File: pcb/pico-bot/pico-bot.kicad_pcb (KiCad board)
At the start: 2 copper layers, 101.6 x 1.7 mm, 62 parts, among them J1 Conn_01x02_Male, J2 Conn_01x06_Male, J3 Conn_01x06_Male, J4 Conn_01x06_Male, J5 Conn_01x06_Male, Q1 DMG2305UX, Q2 AOD417, SW1 SW_SPDT, SW2 SW_Push, SW3 SW_Push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

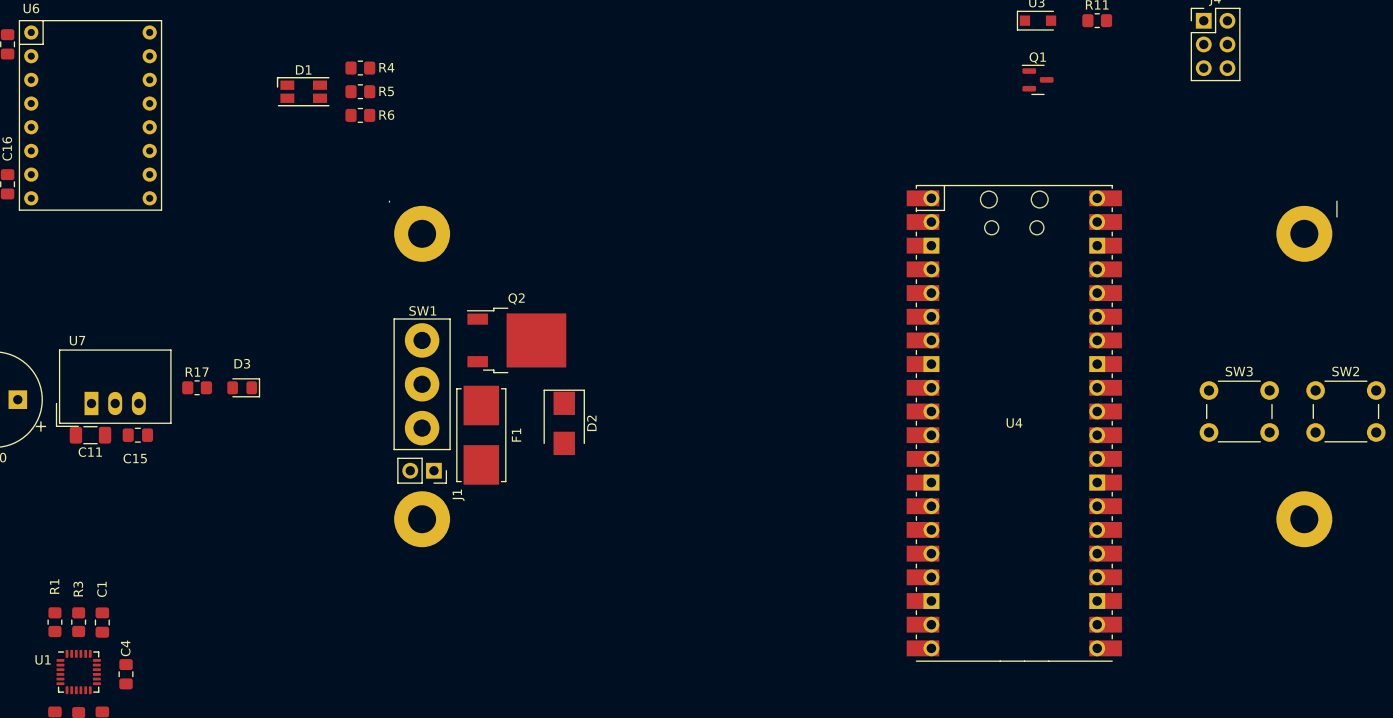
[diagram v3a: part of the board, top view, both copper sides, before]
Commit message: Add rough board outline
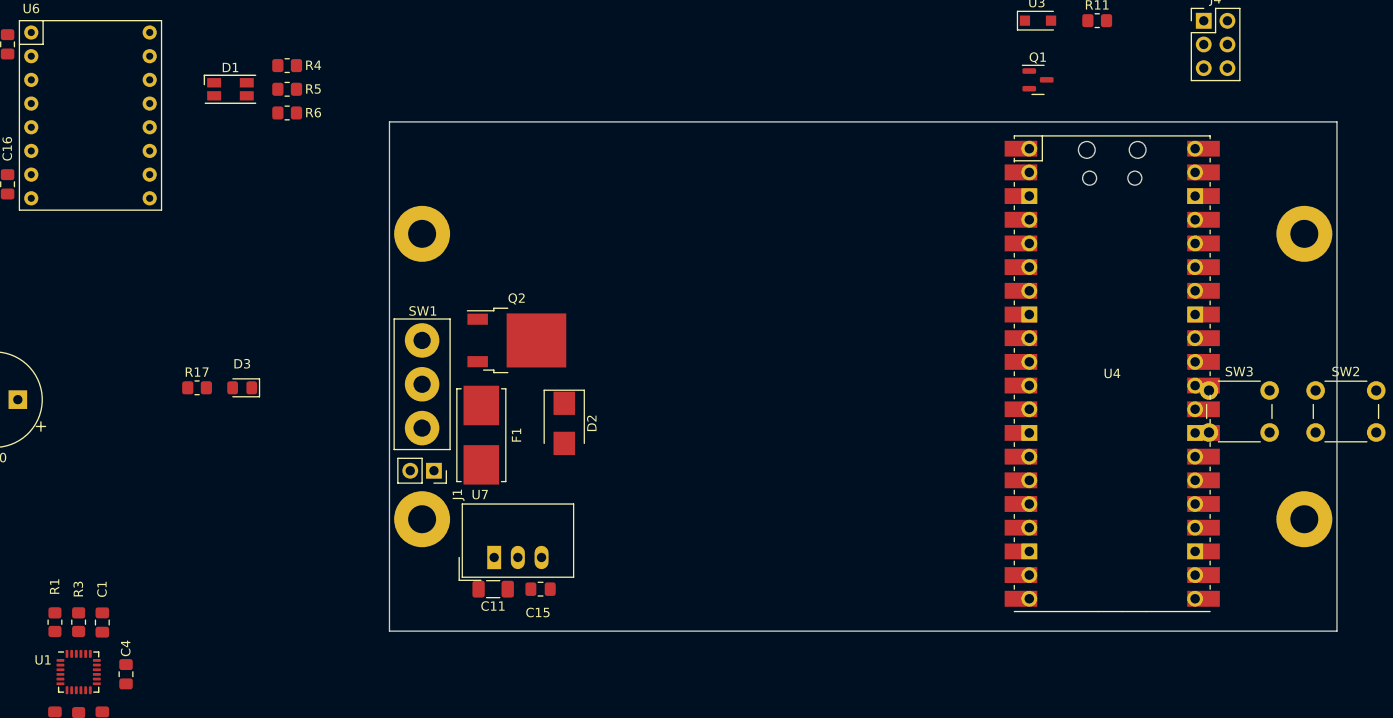
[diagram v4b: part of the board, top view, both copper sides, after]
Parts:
- moved C11 46.2 mm to (108.5, 116.6)
- moved C15 46.2 mm to (113.6, 116.6)
- moved U7 46.2 mm to (108.6, 113.2)
- moved U4 11.8 mm to (174.9, 93.5)
- moved D1 7.85 mm to (80.3, 63.0)
- moved R4 7.85 mm to (86.4, 60.5)
- moved R5 7.85 mm to (86.4, 63.0)
- moved R6 7.85 mm to (86.4, 65.5)
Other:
- board size 101.6 x 1.7 mm -> 101.6 x 54.6 mm
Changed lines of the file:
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@@
   )
   (footprint "pico-bot:RPi_Pico_SMD_TH" (layer "F.Cu")
-    (at 164.4 98.82)
+    (at 174.9 93.5)
     (descr "Through hole straight pin header, 2x20, 2.54mm pitch, double rows")
     (tags "Through hole pin header THT 2x20 2.54mm double row")
@@
   )
   (footprint "LED_SMD:LED_RGB_1210" (layer "F.Cu")
-    (at 88.2 63.26)
+    (at 80.35 63)
     (descr "RGB LED 3.2x2.7mm http://www.avagotech.com/docs/AV02-0610EN")
     (tags "LED 3227")
@@
   )
   (footprint "Resistor_SMD:R_0805_2012Metric_Pad1.20x1.40mm_HandSolder" (layer "F.Cu")
-    (at 94.28 60.72)
+    (at 86.43 60.46)
     (descr "Resistor SMD 0805 (2012 Metric), square (rectangular) end terminal, IPC_7351 nominal with elongated pad for handsoldering. (Body size source: IPC-SM-782 page 72, https://www.pcb-3d.com/wordpress/wp-content/uploads/ipc-sm-782a_amendment_1_and_2.pdf), generated with kicad-footprint-generator")
     (tags "resistor handsolder")
@@
   )
   (footprint "Capacitor_SMD:C_1206_3216Metric_Pad1.33x1.80mm_HandSolder" (layer "F.Cu")
-    (at 65.34 100.09 180)
+    (at 108.52 116.6 180)
     (descr "Capacitor SMD 1206 (3216 Metric), square (rectangular) end terminal, IPC_7351 nominal with elongated pad for handsoldering. (Body size source: IPC-SM-782 page 76, https://www.pcb-3d.com/wordpress/wp-content/uploads/ipc-sm-782a_amendment_1_and_2.pdf), generated with kicad-footprint-generator")
     (tags "capacitor handsolder")
@@
   )
   (footprint "Converter_DCDC:Converter_DCDC_TRACO_TSR-1_THT" (layer "F.Cu")
-    (at 65.4475 96.6925)
+    (at 108.6275 113.2025)
     (descr "DCDC-Converter, TRACO, TSR 1-xxxx")
     (tags "DCDC-Converter TRACO TSR-1")
@@
   )
   (footprint "Capacitor_SMD:C_0805_2012Metric_Pad1.18x1.45mm_HandSolder" (layer "F.Cu")
-    (at 70.42 100.09)
+    (at 113.6 116.6)
     (descr "Capacitor SMD 0805 (2012 Metric), square (rectangular) end terminal, IPC_7351 nominal with elongated pad for handsoldering. (Body size source: IPC-SM-782 page 76, https://www.pcb-3d.com/wordpress/wp-content/uploads/ipc-sm-782a_amendment_1_and_2.pdf, https://docs.google.com/spreadsheets/d/1BsfQQcO9C6DZCsRaXUlFlo91Tg2WpOkGARC1WS5S8t0/edit?usp=sharing), generated with kicad-footprint-generator")
     (tags "capacitor handsolder")
@@
   )
   (footprint "Resistor_SMD:R_0805_2012Metric_Pad1.20x1.40mm_HandSolder" (layer "F.Cu")
-    (at 94.28 65.8)
+    (at 86.43 65.54)
     (descr "Resistor SMD 0805 (2012 Metric), square (rectangular) end terminal, IPC_7351 nominal with elongated pad for handsoldering. (Body size source: IPC-SM-782 page 72, https://www.pcb-3d.com/wordpress/wp-content/uploads/ipc-sm-782a_amendment_1_and_2.pdf), generated with kicad-footprint-generator")
     (tags "resistor handsolder")
@@
   )
   (footprint "Resistor_SMD:R_0805_2012Metric_Pad1.20x1.40mm_HandSolder" (layer "F.Cu")
-    (at 94.28 63.26)
+    (at 86.43 63)
     (descr "Resistor SMD 0805 (2012 Metric), square (rectangular) end terminal, IPC_7351 nominal with elongated pad for handsoldering. (Body size source: IPC-SM-782 page 72, https://www.pcb-3d.com/wordpress/wp-content/uploads/ipc-sm-782a_amendment_1_and_2.pdf), generated with kicad-footprint-generator")
     (tags "resistor handsolder")
@@
     )
   )
-  (gr_line (start 199 76.7) (end 199 75) (layer "Edge.Cuts") (width 0.1))
-  (gr_line (start 97.4 75.1) (end 97.4 75) (layer "Edge.Cuts") (width 0.1))
+  (gr_line (start 199 66.5) (end 97.4 66.5) (layer "Edge.Cuts") (width 0.1))
+  (gr_line (start 199 121.1) (end 199 66.5) (layer "Edge.Cuts") (width 0.1))
+  (gr_line (start 97.4 66.5) (end 97.4 121.1) (layer "Edge.Cuts") (width 0.1))
+  (gr_line (start 97.4 121.1) (end 199 121.1) (layer "Edge.Cuts") (width 0.1))
 )

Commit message: Finish init placement of components
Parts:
- moved J5 146.1 mm to (184.1, 117.2), turned to 90 degrees
- moved C19 123.3 mm to (144.1, 116.6), turned to 0 degrees
- moved J3 122.4 mm to (137.7, 113.4), turned to 90 degrees
- moved D1 121.6 mm to (195.5, 102.0), turned to -90 degrees
- moved R4 113.0 mm to (190.4, 104.5), turned to 180 degrees
- moved R5 111.1 mm to (190.4, 102.0), turned to 180 degrees
- moved R6 109.4 mm to (190.4, 99.5), turned to 180 degrees
- moved C18 101.1 mm to (143.4, 69.6), turned to 0 degrees
- moved J2 99.5 mm to (137.1, 72.8), turned to 90 degrees
- moved C14 93.2 mm to (142.2, 103.3)
- moved C12 93.2 mm to (137.1, 103.3)
- moved C13 93.2 mm to (139.6, 103.3)
- moved C2 90.8 mm to (146.6, 99.1)
- moved C3 90.8 mm to (151.7, 99.1)
- moved R1 90.8 mm to (146.6, 88.4)
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
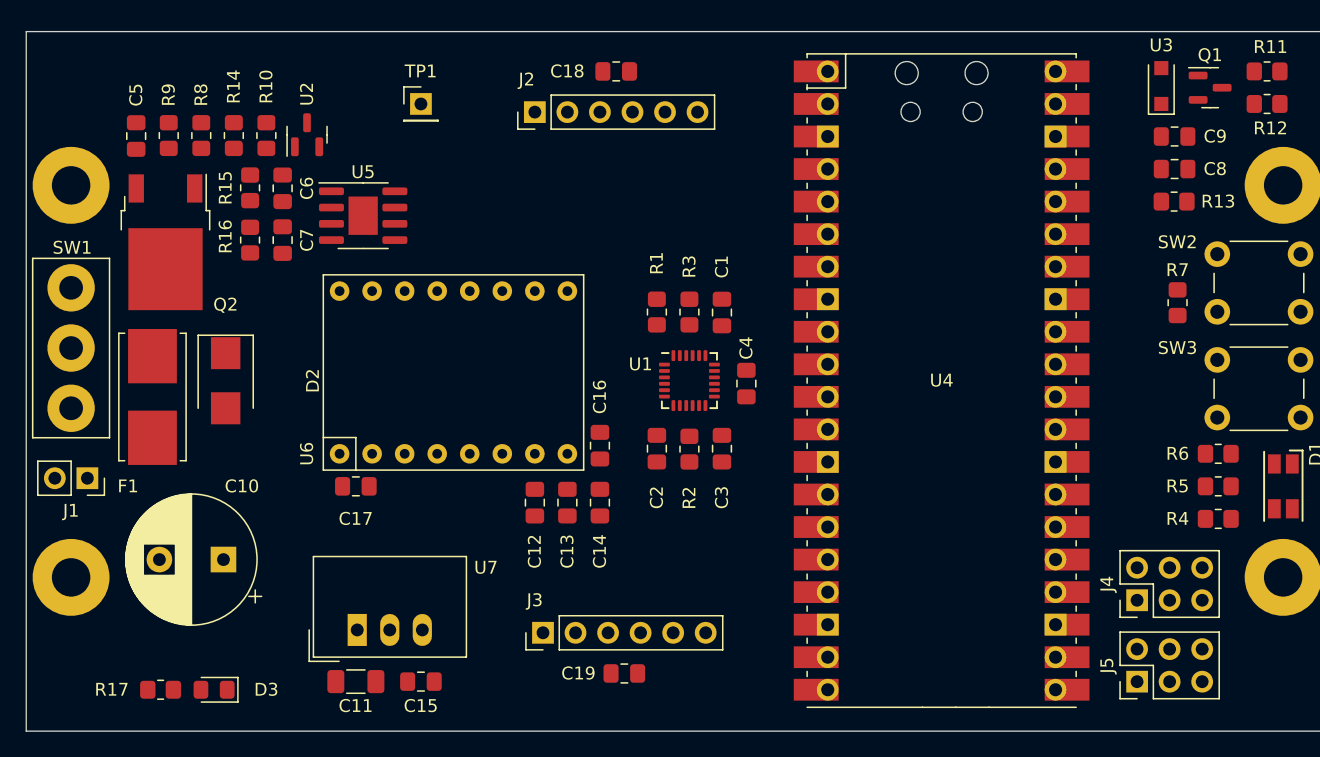
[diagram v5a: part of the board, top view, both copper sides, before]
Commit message: Route power and input protection
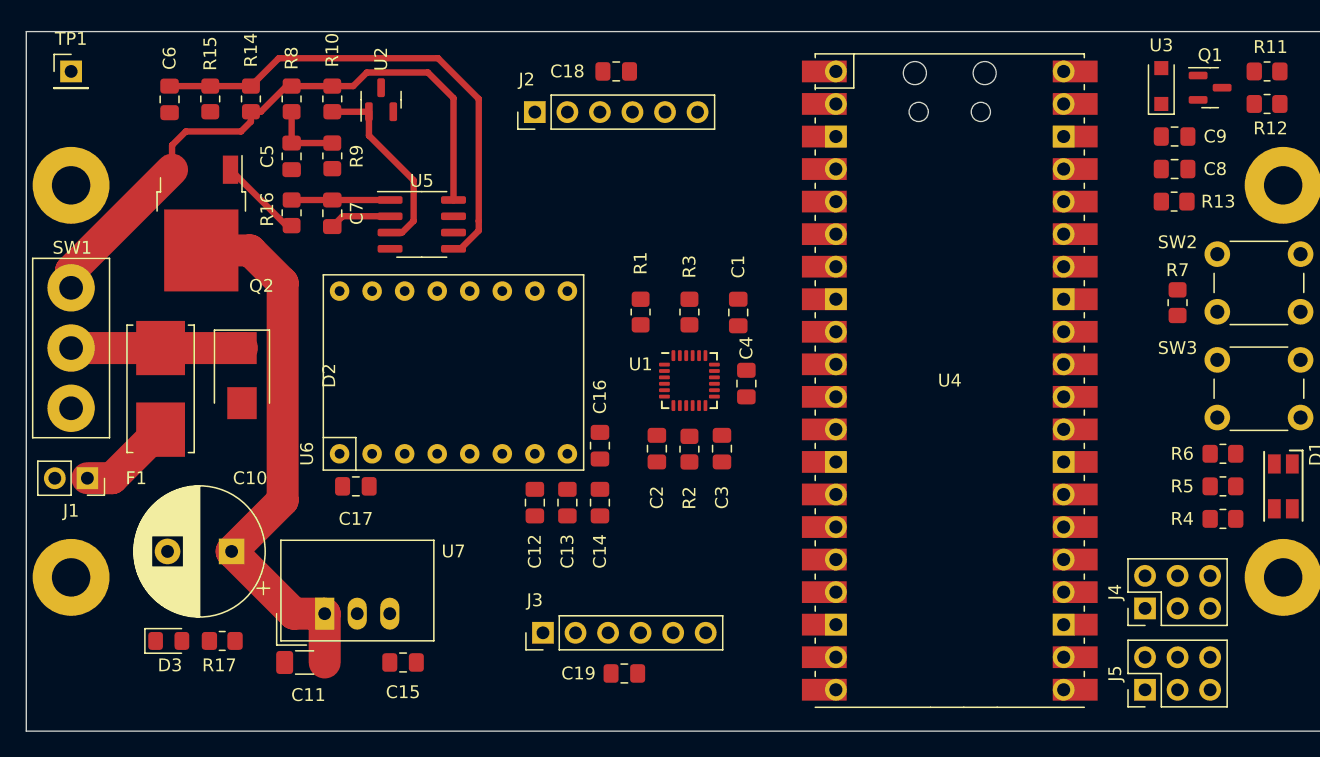
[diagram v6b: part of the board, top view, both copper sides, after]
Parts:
- moved TP1 27.4 mm to (100.9, 69.6)
- moved R9 12.9 mm to (121.3, 76.2)
- moved C5 12.2 mm to (118.1, 76.2)
- moved C6 11.2 mm to (108.6, 71.8)
- moved R8 7.61 mm to (118.1, 71.8)
- moved R15 7.60 mm to (111.8, 71.8)
- moved U2 6.39 mm to (125.1, 71.8)
- moved R17 6.14 mm to (112.7, 114.1), turned to 180 degrees
- moved R10 5.89 mm to (121.3, 71.8)
- moved D3 5.20 mm to (108.5, 114.1), turned to 0 degrees
- moved U5 4.63 mm to (128.3, 81.5)
- moved C7 4.40 mm to (121.3, 80.7)
- moved C11 4.26 mm to (119.1, 115.7), turned to 0 degrees
- moved R16 3.88 mm to (118.1, 80.6)
- moved R14 3.16 mm to (114.9, 71.8), turned to -90 degrees
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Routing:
- net VBAT_UNSW: track 0.00 -> 48.0 mm
- net VBAT: track 0.00 -> 43.1 mm
- net Net-(C6-Pad2): track 0.00 -> 39.2 mm
- net Net-(R10-Pad1): track 0.00 -> 15.0 mm
- net Net-(D2-Pad1): track 0.00 -> 13.3 mm
- net Net-(C5-Pad2): track 0.00 -> 10.5 mm
- net Net-(C7-Pad2): track 0.00 -> 7.69 mm
- net Net-(F1-Pad1): track 0.00 -> 7.28 mm
- net Net-(Q2-Pad1): track 0.00 -> 6.58 mm

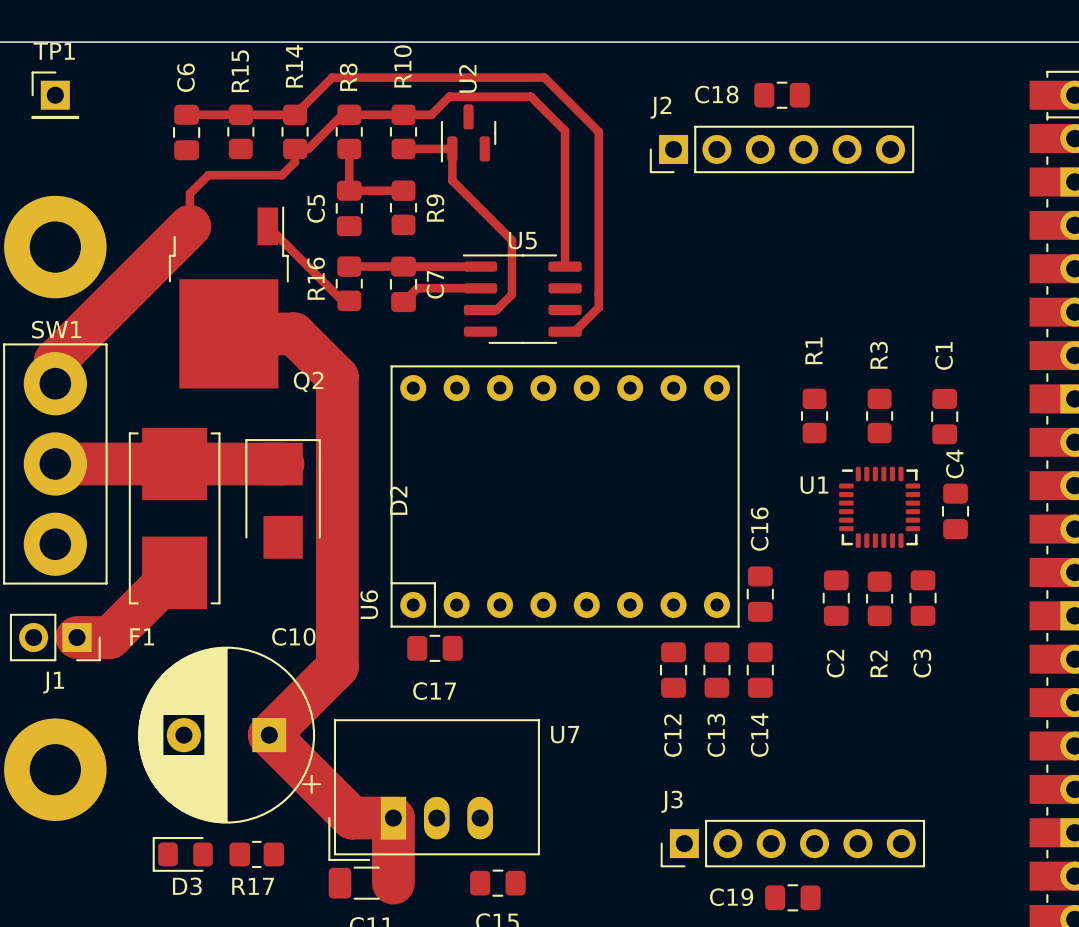
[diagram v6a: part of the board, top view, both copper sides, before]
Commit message: Partial route mpu6050
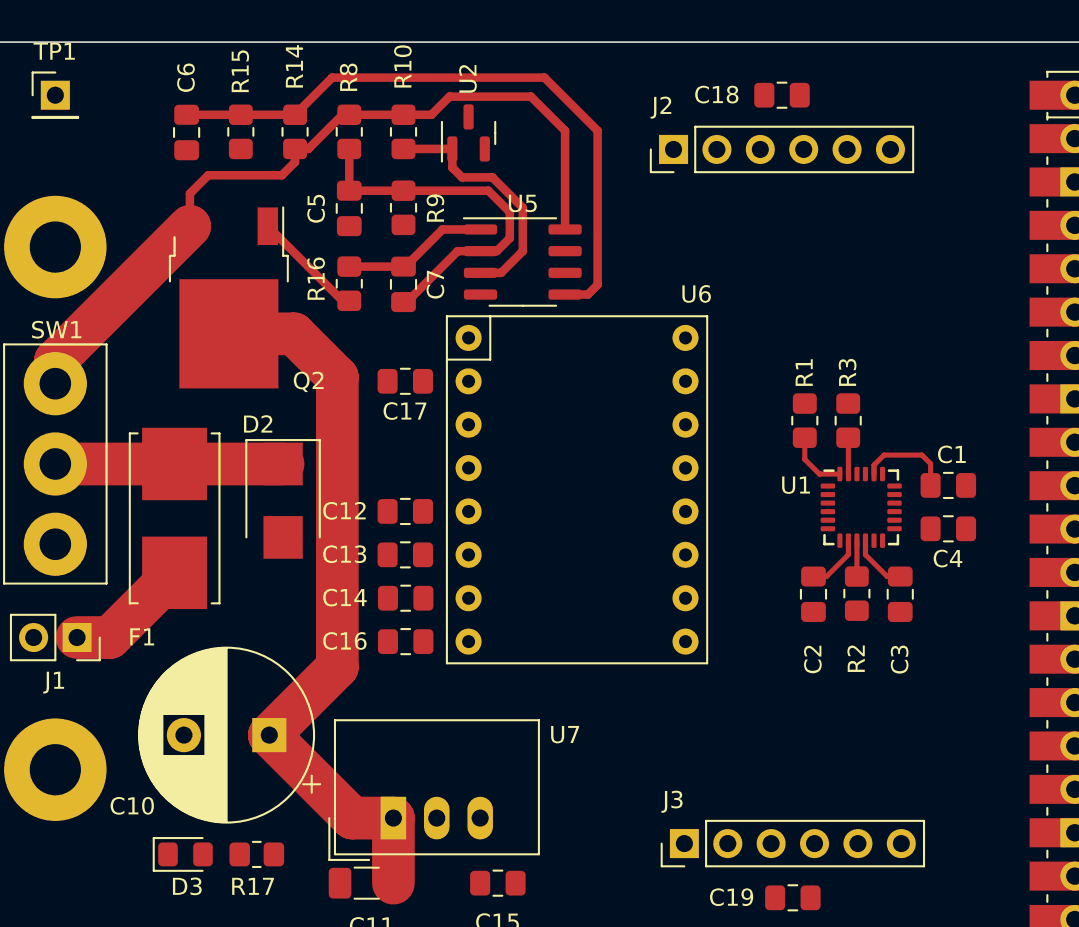
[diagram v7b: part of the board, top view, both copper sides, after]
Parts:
- moved C14 21.2 mm to (121.4, 99.1), turned to 0 degrees
- moved C16 20.9 mm to (121.4, 101.6), turned to 0 degrees
- moved C13 19.5 mm to (121.4, 96.5), turned to 0 degrees
- moved C12 18.2 mm to (121.4, 94.0), turned to 0 degrees
- moved U6 16.0 mm to (125.1, 83.8), turned to 0 degrees
- moved C17 15.7 mm to (121.4, 86.4)
- moved C1 4.03 mm to (153.2, 92.5), turned to 180 degrees
- moved U5 2.17 mm to (128.3, 79.4)
- moved R3 1.86 mm to (147.3, 88.7)
- moved R2 1.37 mm to (147.8, 98.8)
- moved C2 1.35 mm to (145.3, 98.8)
- moved C3 1.35 mm to (150.4, 98.8)
- moved C4 1.11 mm to (153.2, 95.0), turned to 180 degrees
- moved U1 1.08 mm to (148.1, 93.7)
- moved R1 0.63 mm to (144.8, 88.7)
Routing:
- net Net-(C5-Pad2): track 10.5 -> 21.7 mm
- net Net-(C1-Pad2): track 0.00 -> 5.56 mm
- net /SDA: track 0.00 -> 3.68 mm
- net +3V3: track 0.00 -> 3.39 mm
- net Net-(C3-Pad2): track 0.00 -> 3.39 mm
- net VBAT_UNSW: track 48.0 -> 45.8 mm
- net /SCL: track 0.00 -> 2.13 mm
- net Net-(R2-Pad2): track 0.00 -> 2.10 mm
- net Net-(C6-Pad2): track 39.2 -> 37.4 mm
- net Net-(C7-Pad2): track 7.69 -> 8.86 mm
- net /VBAT_MEASURE: track 0.00 -> 0.55 mm
